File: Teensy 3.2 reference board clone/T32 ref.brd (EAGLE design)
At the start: 71.1 x 25.4 mm, 89 parts, among them K1 MK20DX256VLH7, K2 MKL04Z32VLC4, T1 MCP1825S, X1 MINI-USB

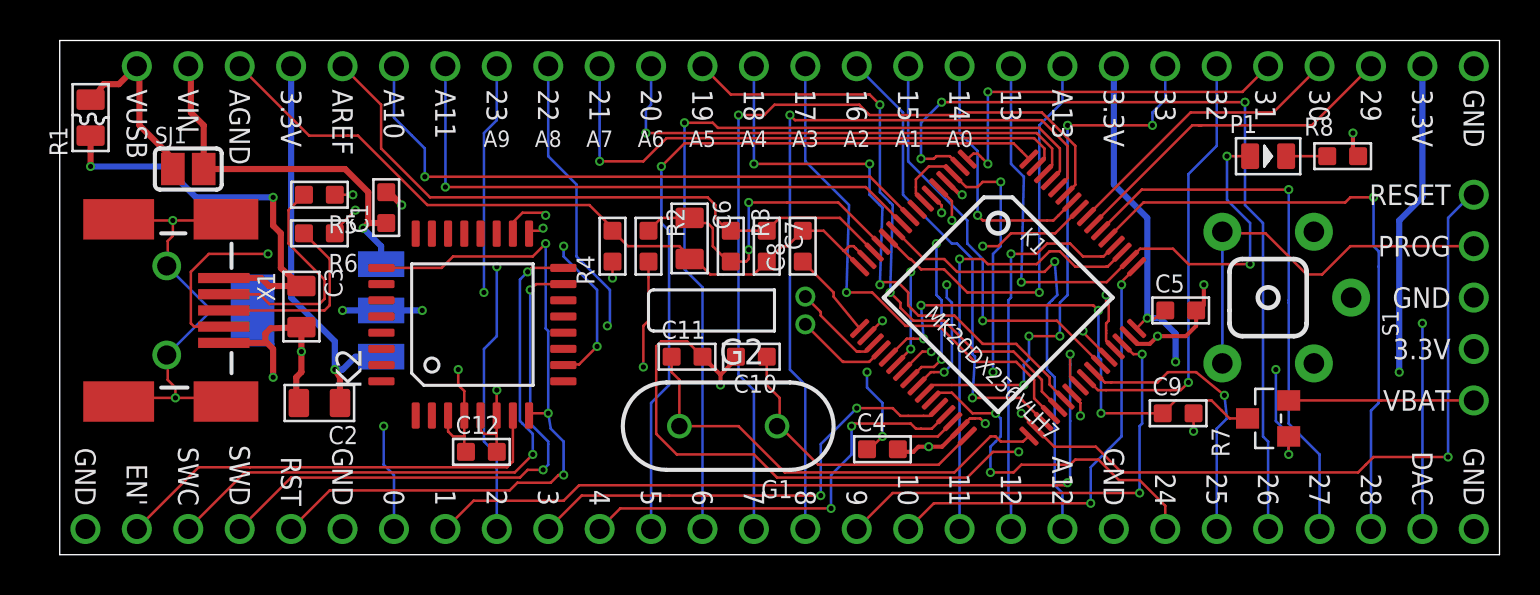
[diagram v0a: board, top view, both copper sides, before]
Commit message: fix wrong ferrite package
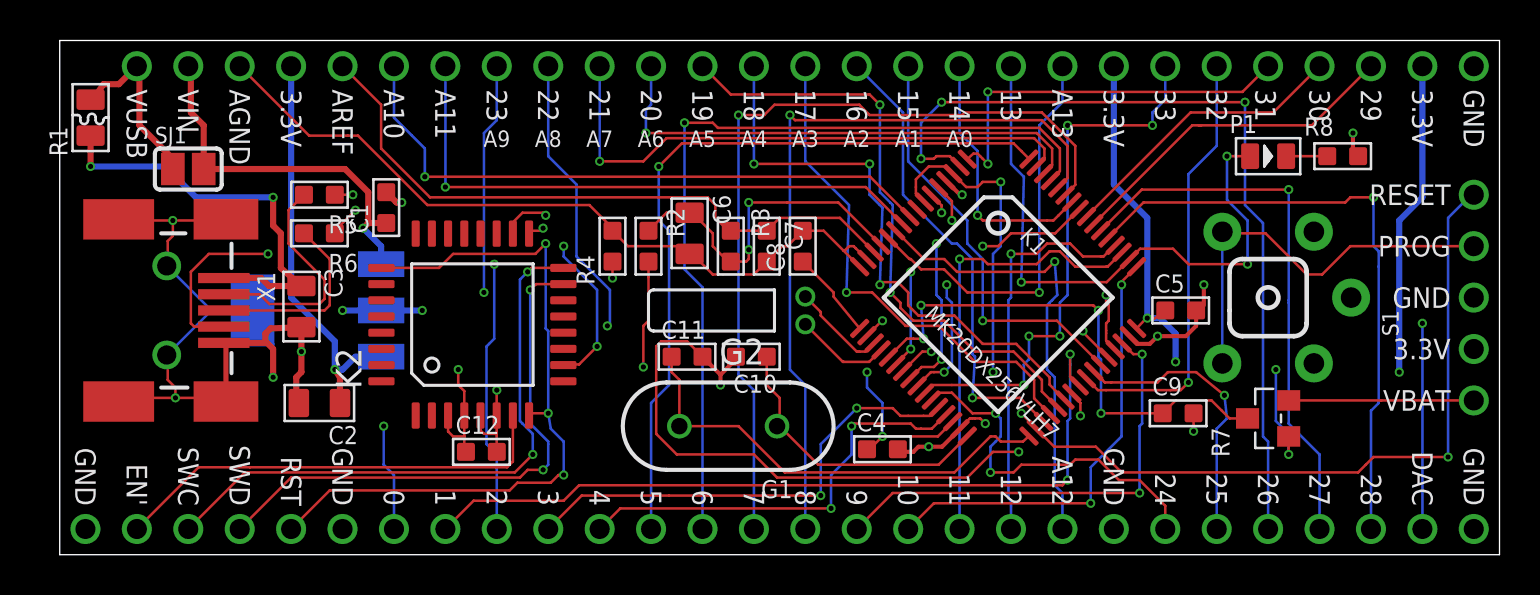
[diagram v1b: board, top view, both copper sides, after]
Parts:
- moved C6 0.25 mm to (31.1, 15.9)
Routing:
- net GND: track 92.2 -> 95.3 mm
